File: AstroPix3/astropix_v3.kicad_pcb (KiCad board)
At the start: 4 copper layers, 51.3 x 48.9 mm, 56 parts, among them J1 pcie_GECCO, J10 SPI_right, J2 ChipRings, J3 TempSens, J3 Vtemp1, J4 SFOut, J5 sample_clock_out, J6 HV_in_external, J9 SPI_left, U1 TLV333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

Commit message: PCB: Astropix3 updates
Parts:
- added C1: 1nF, Capacitor_SMD:C_0603_1608Metric, F.Cu at (171.0, 80.6)
- added C15: 10uF, Capacitor_SMD:C_0603_1608Metric, F.Cu at (188.9, 60.9)
- added C2: .1uF, Capacitor_SMD:C_0603_1608Metric, F.Cu at (188.9, 58.4)
- added J7: HV_in_ring, Connector_Coaxial:SMA_Molex_73251-2200_Horizontal, F.Cu at (173.9, 74.6)
- added R15: 220k, Resistor_SMD:R_0603_1608Metric, F.Cu at (184.9, 60.9)
- added R16: 220k, Resistor_SMD:R_0603_1608Metric, F.Cu at (180.9, 60.9)
- added R19: 220k, Resistor_SMD:R_0603_1608Metric, F.Cu at (184.9, 58.4)
- added R6: 220k, Resistor_SMD:R_0603_1608Metric, F.Cu at (180.9, 58.4)
- added R9: 220k, Resistor_SMD:R_0603_1608Metric, F.Cu at (192.9, 58.4)
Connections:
- J1 pad A5: unconnected-(J1-PadA5) -> VSSA

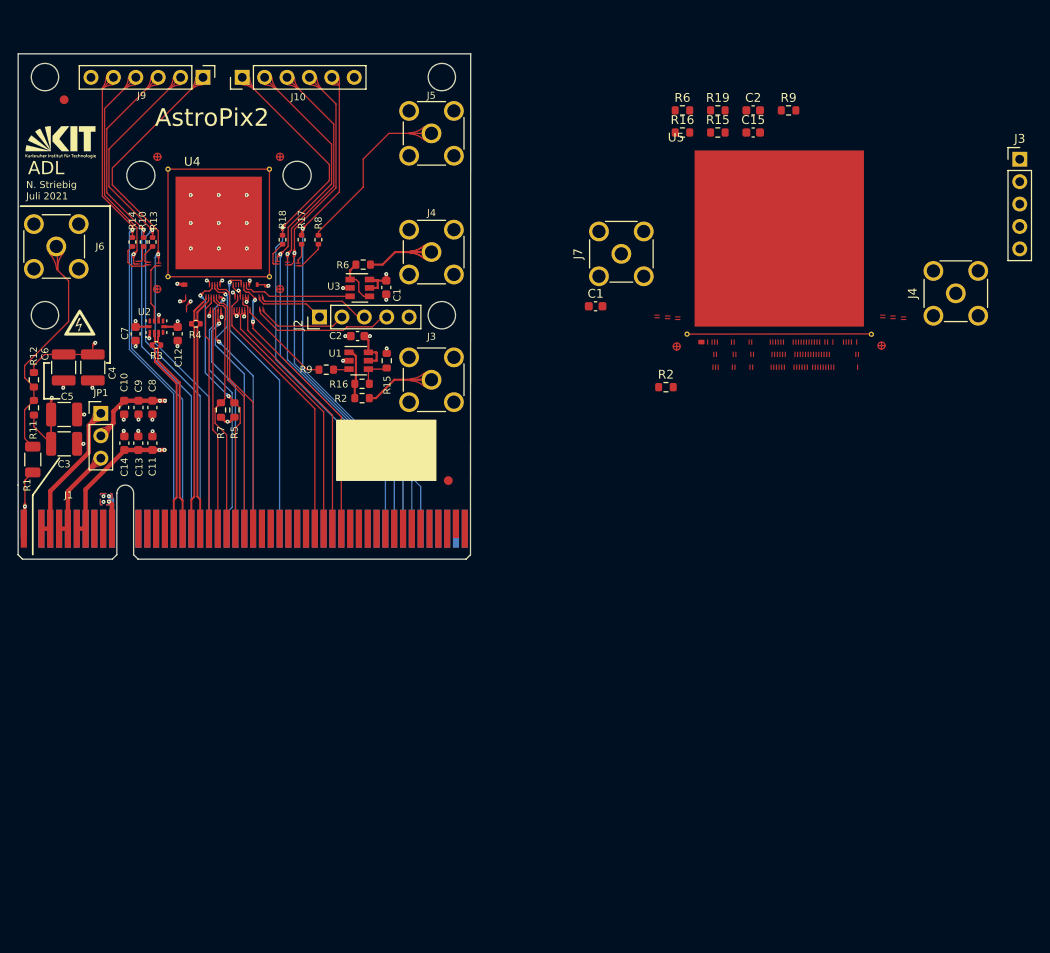
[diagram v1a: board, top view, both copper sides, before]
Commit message: PCB: Astropix3 update
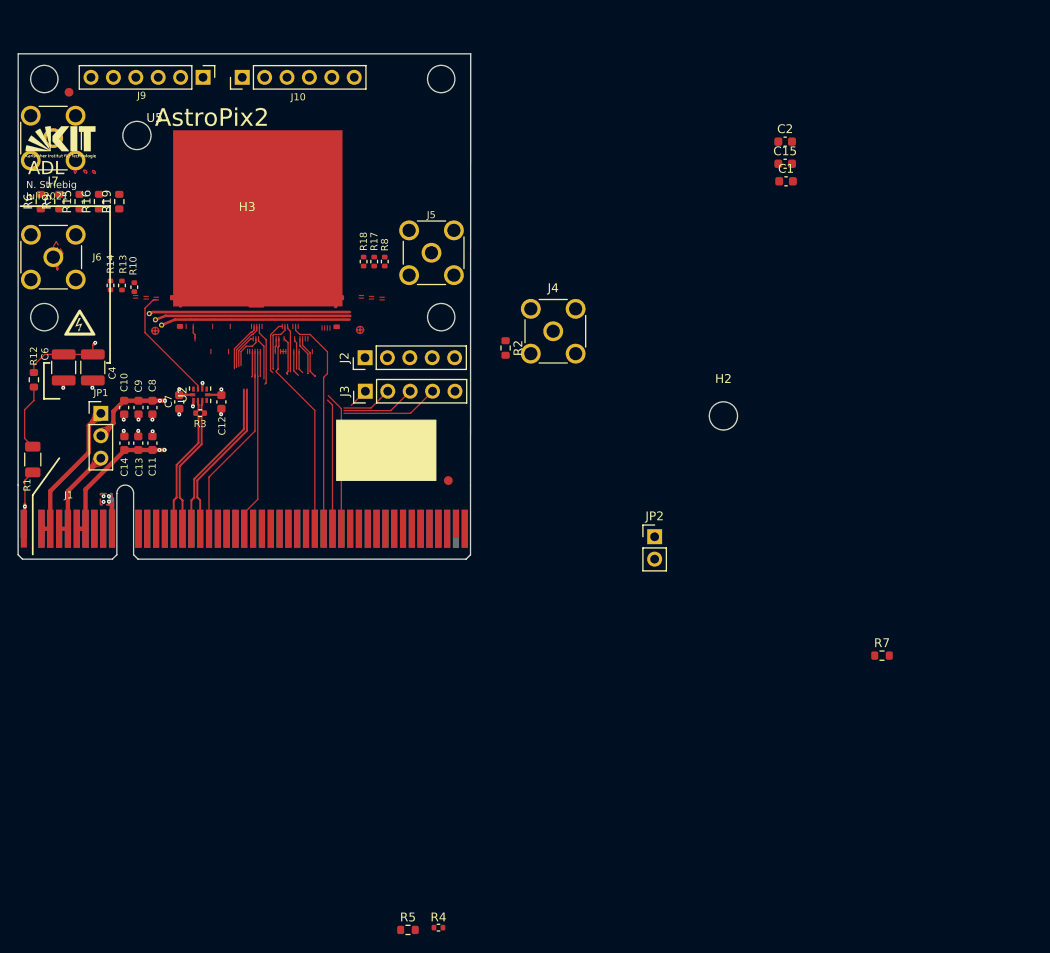
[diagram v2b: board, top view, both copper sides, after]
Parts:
- removed the C1 at (147.3, 78.4)
- removed the C2 at (144.0, 83.9)
- removed C3: 1nF, Capacitor_SMD:C_1210_3225Metric
- removed C5: .1uF, Capacitor_SMD:C_1210_3225Metric
- removed the J3 at (152.4, 88.9)
- removed the J4 at (152.4, 74.4)
- removed R11: 1k, Resistor_SMD:R_0603_1608Metric
- removed the R15 at (147.3, 86.7)
- removed the R16 at (144.5, 89.4)
- removed the R2 at (144.5, 91.0)
- removed the R6 at (144.7, 75.8)
- removed the R9 at (140.5, 87.8)
- removed U1: TLV333, Package_TO_SOT_SMD:SOT-23-6
- removed U3: OPA320S, Package_TO_SOT_SMD:SOT-23-6
- removed U4: AstroPix2_split, astropix:AstroPix2
- added JP2: Jumper_2_Open, Connector_PinHeader_2.54mm:PinHeader_1x02_P2.54mm_Vertical, F.Cu at (177.7, 106.7)
- U2: footprint astropix:Texas_Instruments-SN65LVDS4RSET-0 -> Package_DFN_QFN:Texas_R-PUQFN-N10
- U5: footprint astropix:AstroPix3 -> astropix:AstroPix3_power
- moved R9 83.3 mm to (110.2, 68.7), turned to 90 degrees
- moved R7 80.0 mm to (203.5, 120.2), turned to 0 degrees
- moved J3 78.7 mm to (144.9, 90.2), turned to 90 degrees
- moved R4 73.8 mm to (153.2, 151.0)
- moved R6 73.5 mm to (108.1, 68.7), turned to 90 degrees
- moved R15 72.8 mm to (112.5, 68.7), turned to 90 degrees
- moved R19 68.6 mm to (117.0, 68.7), turned to 90 degrees
- moved R16 66.6 mm to (114.7, 68.7), turned to 90 degrees
- moved J7 65.7 mm to (109.5, 61.5), turned to 90 degrees
- moved R5 62.1 mm to (149.7, 151.3), turned to 0 degrees
- moved U5 59.2 mm to (123.4, 80.4)
- moved H2 55.5 mm to (185.5, 93.0)
- moved J4 45.9 mm to (166.2, 83.4), turned to -90 degrees
- moved C1 25.8 mm to (192.6, 66.4)
- moved R2 18.7 mm to (160.8, 85.3), turned to -90 degrees
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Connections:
- J1 pad A32: unconnected-(J1-PadA32) -> /DAC_ThPMOS
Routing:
- net /spi_right_clk: track 63.8 -> 0.00 mm, vias 1 -> 0
- net /spi_right_miso1: track 63.1 -> 0.00 mm, vias 1 -> 0
- net /spi_right_miso0: track 61.9 -> 0.00 mm, vias 1 -> 0
- net /spi_right_csn: track 61.8 -> 0.00 mm, vias 1 -> 0
- net /spi_left_mosi: track 61.3 -> 0.00 mm, vias 1 -> 0
- net /spi_left_miso0: track 60.3 -> 0.00 mm, vias 1 -> 0
- net /spi_right_mosi: track 59.6 -> 0.00 mm, vias 1 -> 0
- net /spi_left_miso1: track 58.6 -> 0.00 mm, vias 1 -> 0
- net /spi_left_clk: track 58.4 -> 0.00 mm, vias 1 -> 0
- net /spi_left_csn: track 56.2 -> 0.00 mm, vias 1 -> 0
- net /res_n: track 30.7 -> 4.00 mm, vias 2 -> 0
- net /sr_ck1: track 30.5 -> 4.14 mm, vias 1 -> 0
- net /interrupt: track 29.0 -> 2.94 mm
- net /Inj: track 32.2 -> 6.13 mm, vias 1 -> 0
- net /sr_out: track 28.6 -> 2.81 mm, vias 1 -> 0
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- added copper zone on In2.Cu, net (none)
- removed copper zone on In2.Cu, net subd

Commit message: PCB: Astropix3 update
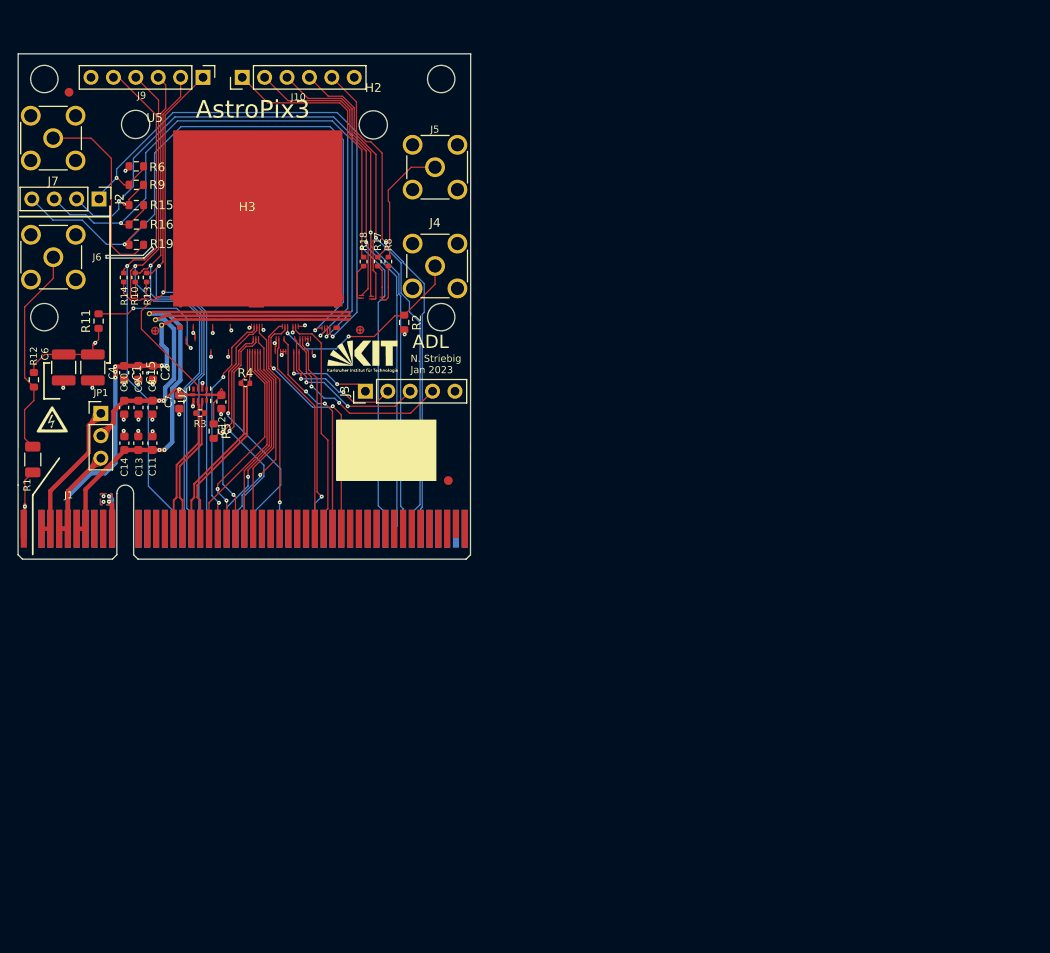
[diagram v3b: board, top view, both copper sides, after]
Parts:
- removed JP2: Jumper_2_Open, Connector_PinHeader_2.54mm:PinHeader_1x02_P2.54mm_Vertical
- removed R7: 10k, Resistor_SMD:R_0603_1608Metric
- added R11: 0, Resistor_SMD:R_0603_1608Metric, F.Cu at (114.7, 82.2)
- J2: footprint Connector_PinHeader_2.54mm:PinHeader_1x05_P2.54mm_Vertical -> Connector_PinHeader_2.54mm:PinHeader_1x04_P2.54mm_Vertical
- moved C1 78.1 mm to (117.5, 88.1), turned to -90 degrees
- moved C15 77.1 mm to (119.2, 88.1), turned to -90 degrees
- moved C2 76.3 mm to (120.8, 88.1), turned to -90 degrees
- moved R4 65.5 mm to (131.3, 89.3)
- moved R5 60.7 mm to (127.7, 94.7), turned to -90 degrees
- moved H2 51.6 mm to (145.8, 60.0)
- moved Logo1 42.0 mm to (144.6, 86.3)
- moved J2 35.1 mm to (114.7, 68.4), turned to -90 degrees
- moved J4 15.3 mm to (152.8, 76.0)
- moved R2 11.9 mm to (149.3, 82.4)
- moved R6 11.5 mm to (118.9, 64.7), turned to 0 degrees
- moved Logo2 11.4 mm to (109.4, 93.4)
- moved J5 9.71 mm to (152.8, 64.8)
- moved R9 8.93 mm to (118.9, 66.8), turned to 0 degrees
- moved R15 6.44 mm to (118.9, 69.1), turned to 0 degrees
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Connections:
- J1 pad A6: unconnected-(J1-PadA6) -> VSSA
- J2 pad 2: /ring4 -> /ring2
- J2 pad 4: /ring2 -> /ring4
- U5 pad B5: suba -> Net-(R11-Pad2)
- U5 pad VDDA_Ring: (no net) -> VDDA
- U5 pad VDDD_Ring: (no net) -> VDD
- U5 pad VSSA_Ring: (no net) -> VSSA
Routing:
- net /ring4: track 0.00 -> 75.0 mm, vias 0 -> 2
- net /ring3: track 0.00 -> 71.8 mm, vias 0 -> 2
- net /ring2: track 0.00 -> 69.4 mm, vias 0 -> 2
- net /spi_right_miso1: track 0.00 -> 67.5 mm, vias 0 -> 1
- net /spi_right_miso0: track 0.00 -> 66.1 mm, vias 0 -> 1
- net /spi_right_csn: track 0.00 -> 65.4 mm, vias 0 -> 1
- net /ring1: track 0.00 -> 65.0 mm, vias 0 -> 2
- net /spi_right_clk: track 0.00 -> 64.5 mm, vias 0 -> 1
- net /spi_left_clk: track 0.00 -> 64.0 mm, vias 0 -> 1
- net /spi_left_miso1: track 0.00 -> 59.6 mm, vias 0 -> 1
- net /spi_left_csn: track 0.00 -> 58.8 mm, vias 0 -> 1
- net /spi_left_miso0: track 0.00 -> 58.6 mm, vias 0 -> 1
- net /spi_right_mosi: track 0.00 -> 58.0 mm, vias 0 -> 1
- net /spi_left_mosi: track 0.00 -> 57.8 mm, vias 0 -> 1
- net VSSA: track 0.00 -> 34.5 mm, vias 0 -> 5
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- added copper zone on In2.Cu, net GND
- removed copper zone on In2.Cu, net (none)
- removed copper zone on In2.Cu, net VDD
- removed copper zone on In2.Cu, net VDDA
- removed copper zone on In2.Cu, net suba
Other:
- outline, holes or cut-outs redrawn
- board text added: "AstroPix3"
- board text added: "N. Striebig Jan 2023"
- board text removed: "AstroPix2"
- board text removed: "N. Striebig Juli 2021"

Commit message: PCB: Added final V3 PCB with fabrication data
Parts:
- J7: value HV_in_ring -> Conn_01x03; footprint Connector_Coaxial:SMA_Molex_73251-2200_Horizontal -> Connector_PinHeader_2.54mm:PinHeader_1x03_P2.54mm_Vertical
- U5: footprint astropix:AstroPix3_power -> astropix:AstroPix3_power2
- moved H2 26.6 mm to (146.0, 86.6)
- moved Logo1 12.4 mm to (136.9, 96.0)
- moved J3 10.6 mm to (154.6, 86.0), turned to 0 degrees
- moved J7 4.12 mm to (112.7, 64.1), turned to -90 degrees
- moved R6 0.10 mm to (118.9, 64.6)
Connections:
- J1 pad B40: unconnected-(J1-PadB40) -> /DigInj
- J7 pad 1: Net-(J7-Pad1) -> Net-(R6-Pad1)
- R19 pad 2: Net-(J7-Pad1) -> Net-(R19-Pad2)
- R6 pad 1: GND -> Net-(R6-Pad1)
- U5 pad B84: unconnected-(U5-PadB84) -> /DigInj
- U5 pad B85: VDD -> (no net)
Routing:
- net suba: track 11.2 -> 95.3 mm, vias 1 -> 4
- net /DigInj: track 0.00 -> 26.9 mm, vias 0 -> 2
- net Net-(J7-Pad1): track 22.0 -> 0.00 mm
- net Net-(R19-Pad2): track 0.00 -> 21.0 mm
- net Net-(J3-Pad1): track 11.4 -> 22.1 mm
- net Net-(J3-Pad2): track 16.3 -> 23.2 mm
- net Net-(R6-Pad1): track 0.00 -> 5.65 mm
- net Net-(J3-Pad3): track 17.4 -> 21.7 mm
- net Net-(J3-Pad4): track 22.0 -> 23.4 mm
- net /ring2: track 69.4 -> 68.3 mm
- net VDD: track 34.5 -> 33.5 mm, vias 3 -> 2
- net /ring4: track 75.0 -> 74.3 mm
- net /sr_ck2: track 28.3 -> 27.7 mm
- net /spi_right_csn: track 65.4 -> 64.8 mm
- net GND: track 25.6 -> 25.0 mm, vias 34 -> 33
- added copper zone on F.Cu, net VSSA
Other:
- outline, holes or cut-outs redrawn
